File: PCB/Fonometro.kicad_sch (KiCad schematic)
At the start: 68 parts, among them J1 Conn_01x15_Male, J2 Conn_01x15_Male, J3 Power, J4 Conn_01x05_Female, J5 Conn_01x01_Female, U1 LM324, U2 LM358, U3 ESP32-DEVKIT-V1

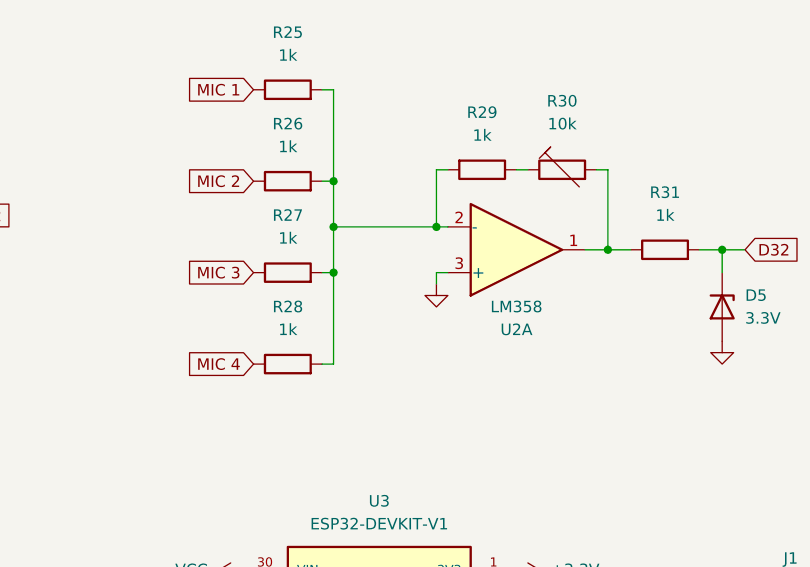
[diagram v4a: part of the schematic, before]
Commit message: fix: now U2A.+ is connected to 1.65V.
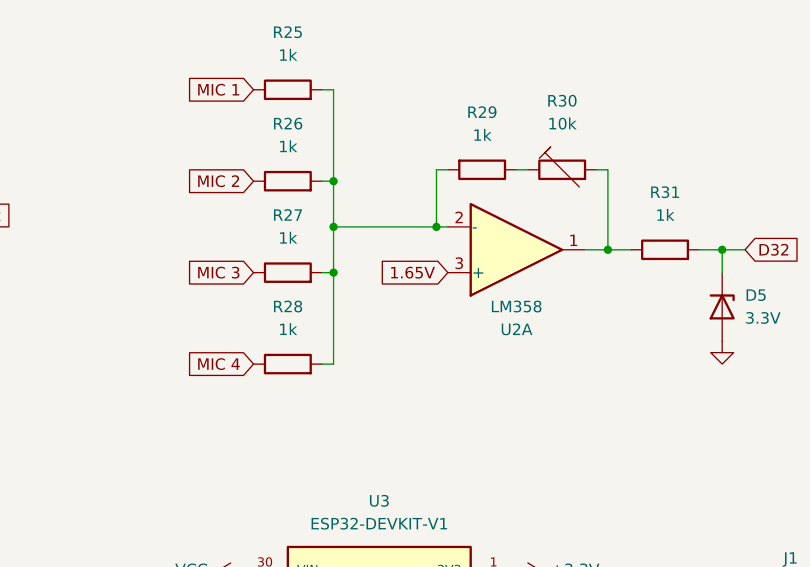
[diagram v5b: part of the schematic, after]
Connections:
- net 1.65V: now also U2.3 (+)
- net GND: no longer U2.3 (+)
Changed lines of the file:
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@@
-    (stroke (width 0) (type default) (color 0 0 0 0))
-  )
-  (wire (pts (xy 140.97 91.44) (xy 140.97 90.17))
     (stroke (width 0) (type default) (color 0 0 0 0))
   )
@@
     (stroke (width 0) (type default) (color 0 0 0 0))
   )
-  (wire (pts (xy 140.97 90.17) (xy 142.24 90.17))
-    (stroke (width 0) (type default) (color 0 0 0 0))
-  )
   (wire (pts (xy 83.82 129.54) (xy 86.36 129.54))
     (stroke (width 0) (type default) (color 0 0 0 0))
@@
     (effects (font (size 1.27 1.27)) (justify right))
     (property "Intersheet References" "${INTERSHEET_REFS}" (id 0) (at 246.0836 78.6606 0)
+      (effects (font (size 1.27 1.27)) (justify right) hide)
+    )
+  )
+  (global_label "1.65V" (shape input) (at 142.24 90.17 180) (fields_autoplaced)
+    (effects (font (size 1.27 1.27)) (justify right))
+    (property "Intersheet References" "${INTERSHEET_REFS}" (id 0) (at 134.505 90.0906 0)
       (effects (font (size 1.27 1.27)) (justify right) hide)
     )
@@
     )
     (property "Datasheet" "" (id 3) (at 222.25 92.71 0)
-      (effects (font (size 1.27 1.27)) hide)
-    )
-    (pin "1")
-  )
-  (symbol (lib_id "power:GND") (at 140.97 91.44 0) (unit 1)
-    (in_bom yes) (on_board yes) (fields_autoplaced)
-    (property "Reference" "#PWR020" (id 0) (at 140.97 97.79 0)
-      (effects (font (size 1.27 1.27)) hide)
-    )
-    (property "Value" "GND" (id 1) (at 140.97 96.52 0)
-      (effects (font (size 1.27 1.27)) hide)
-    )
-    (property "Footprint" "" (id 2) (at 140.97 91.44 0)
-      (effects (font (size 1.27 1.27)) hide)
-    )
-    (property "Datasheet" "" (id 3) (at 140.97 91.44 0)
       (effects (font (size 1.27 1.27)) hide)
     )
@@
       (reference "#PWR019") (unit 1) (value "VCC") (footprint "")
     )
-    (path "/5d71629b-ddcf-4d30-af18-6c8538cb9e74"
-      (reference "#PWR020") (unit 1) (value "GND") (footprint "")
-    )
     (path "/3d2c6127-cf9e-409f-8117-f35a62c1722c"
